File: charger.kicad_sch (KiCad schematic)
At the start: 0 parts

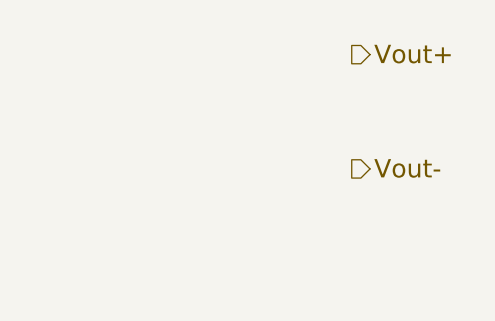
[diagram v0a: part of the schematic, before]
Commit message: Add analog schematic and refine wiring on top.
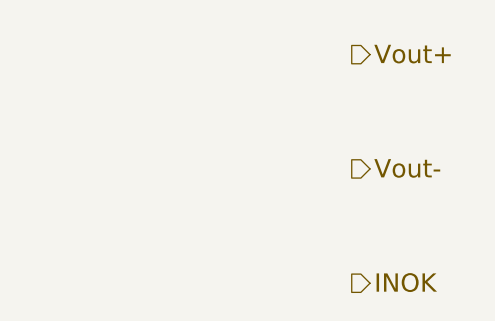
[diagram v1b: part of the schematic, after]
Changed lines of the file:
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@@
+		)
+	)
+	(hierarchical_label "INOK"
+		(shape output)
+		(at 254 63.5 0)
+		(effects
+			(font
+				(size 2.032 2.032)
+			)
+			(justify left)
 		)
 	)

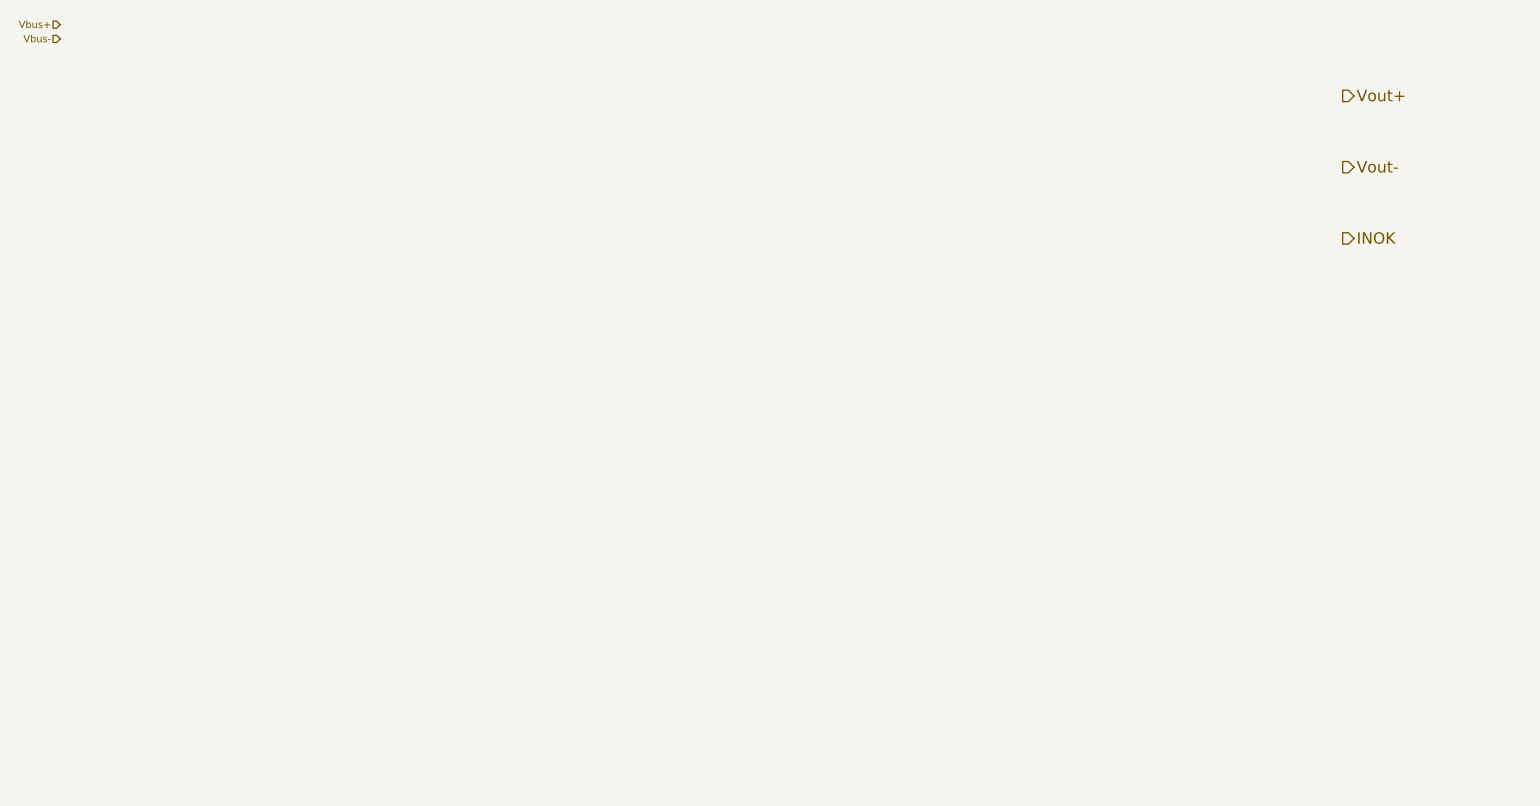
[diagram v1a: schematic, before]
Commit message: Add charger, battery cell.
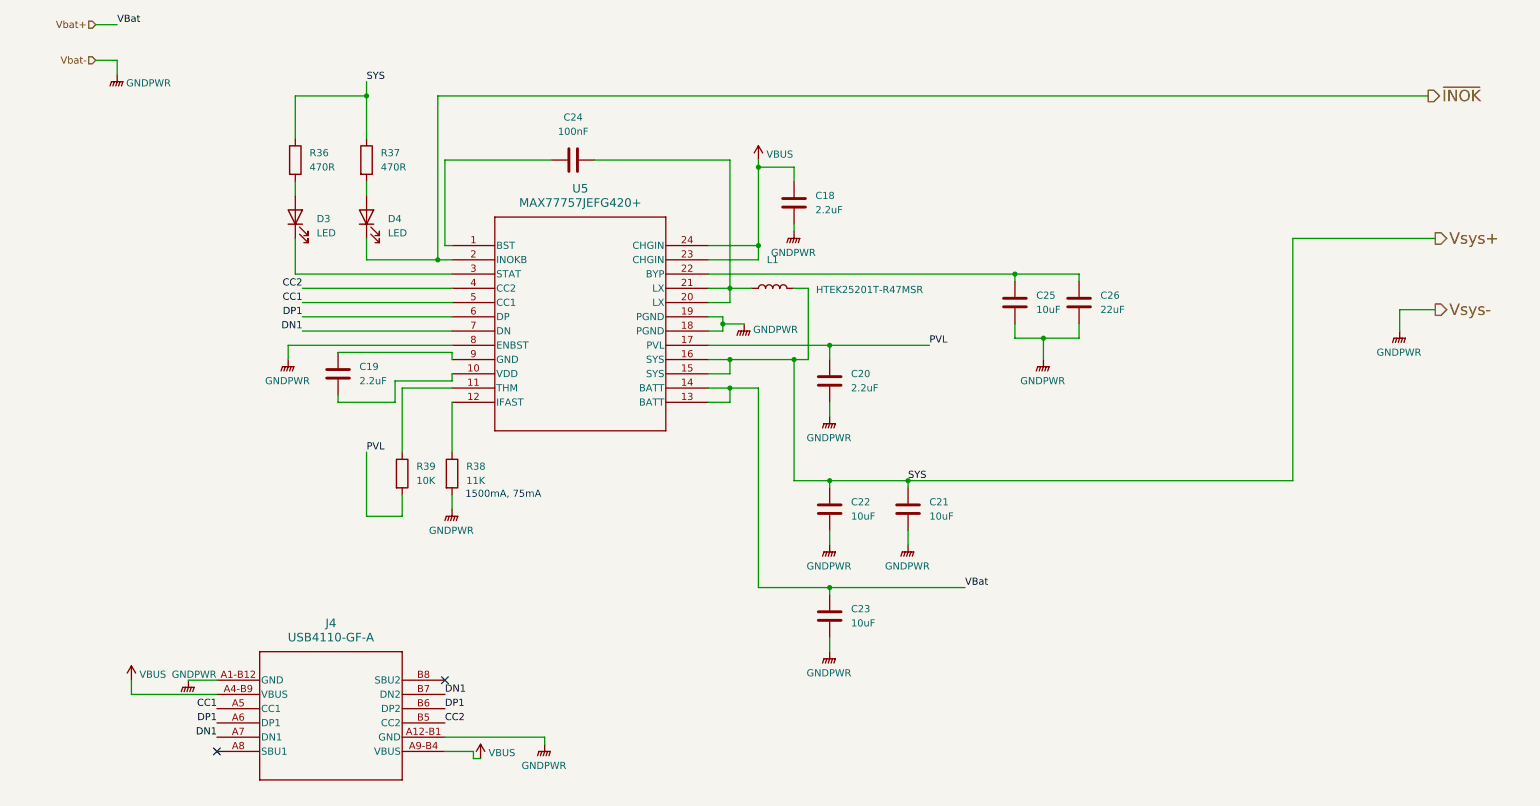
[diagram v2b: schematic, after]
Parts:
- added C18, C19, C20: 2.2uF, Capacitor_SMD:C_0603_1608Metric_Pad1.08x0.95mm_HandSolder, symbol Device:C
- added C21, C22, C23, C25: 10uF, Capacitor_SMD:C_0603_1608Metric_Pad1.08x0.95mm_HandSolder, symbol Device:C
- added C24: 100nF, Capacitor_SMD:C_0603_1608Metric_Pad1.08x0.95mm_HandSolder, symbol Device:C
- added C26: 22uF, Capacitor_SMD:C_0603_1608Metric_Pad1.08x0.95mm_HandSolder, symbol Device:C
- added D3, D4: LED, symbol Device:LED
- added J4: USB4110-GF-A, custom:USB4110-GF-A_GCT, symbol custom:USB4110-GF-A
- added L1: HTEK25201T-R47MSR, Inductor_SMD:L_1008_2520Metric_Pad1.43x2.20mm_HandSolder, symbol Device:L
- added R36, R37: 470R, Resistor_SMD:R_0603_1608Metric_Pad0.98x0.95mm_HandSolder, symbol Device:R
- added R38: 11K, Resistor_SMD:R_0603_1608Metric_Pad0.98x0.95mm_HandSolder, symbol Device:R
- added R39: 10K, Resistor_SMD:R_0603_1608Metric_Pad0.98x0.95mm_HandSolder, symbol Device:R
- added U5: MAX77757JEFG420+, 21-100385B_90-100128_MXM, symbol custom:MAX77757HEFG360+
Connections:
- new net: R38.1, U5.12 (IFAST)
- new net: C25.2, C26.2, U5.22 (BYP)
- new net: D3.2 (A), R36.2
- new net: R39.1, U5.11 (THM)
- new net: C19.1, U5.10 (VDD)
- new net: C19.2, U5.9 (GND)
- new net: D4.2 (A), R37.2
- new net: D3.1 (K), U5.3 (STAT)
- new net: C24.1, L1.1, U5.20 (LX), U5.21 (LX)
- new net: C24.2, U5.1 (BST)
- new net CC1: J4.A5 (CC1), U5.5 (CC1)
- new net CC2: J4.B5 (CC2), U5.4 (CC2)
- new net DN1: J4.A7 (DN1), J4.B7 (DN2), U5.7 (DN)
- new net DP1: J4.A6 (DP1), J4.B6 (DP2), U5.6 (DP)
- new net GNDPWR: C18.1, C20.1, C21.1, C22.1, C23.1, C25.1, C26.1, J4.A1-B12 (GND), J4.A12-B1 (GND), R38.2, U5.18 (PGND), U5.19 (PGND), U5.8 (ENBST)
- new net PVL: C20.2, R39.2, U5.17 (PVL)
- new net VBUS: C18.2, J4.A4-B9 (VBUS), J4.A9-B4 (VBUS), U5.23 (CHGIN), U5.24 (CHGIN)
- new net Vbat+: C23.2, U5.13 (BATT), U5.14 (BATT)
- new net Vsys+: C21.2, C22.2, L1.2, R36.1, R37.1, U5.15 (SYS), U5.16 (SYS)
- new net ~{INOK}: D4.1 (K), U5.2 (INOKB)
- no-connect marks 0 -> 2
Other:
- note added: "1500mA, 75mA"

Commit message: Add console port.
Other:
- note added: "This charger module circuit has not been tested yet."
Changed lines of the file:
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@@
+		)
+	)
+	(text "This charger module circuit has not been tested yet."
+		(exclude_from_sim no)
+		(at 203.708 161.544 0)
+		(effects
+			(font
+				(size 1.27 1.27)
+				(color 194 0 0 1)
+			)
 		)
 	)

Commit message: Fix issues
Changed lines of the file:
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@@
 		(dnp no)
 		(property "Reference" "L1"
-			(at 152.4 67.31 90)
+			(at 160.274 70.866 90)
 			(show_name no)
 			(do_not_autoplace no)

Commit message: Placement concept is finished.
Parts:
- D3, D4: footprint (none) -> LED_SMD:LED_0603_1608Metric
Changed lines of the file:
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@@
 			)
 		)
-		(property "Footprint" ""
+		(property "Footprint" "LED_SMD:LED_0603_1608Metric"
 			(at 80.01 59.69 0)
 			(hide yes)
@@
 			)
 		)
-		(property "Footprint" ""
+		(property "Footprint" "LED_SMD:LED_0603_1608Metric"
 			(at 67.31 59.69 0)
 			(hide yes)

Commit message: Add wiring, change footprint to avoid fatal errors at pads.
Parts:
- renumbered C19 to C18, C24 to C19, C18 to C20, C20 to C21, C21 to C24, D3 to D4, D4 to D5, J4 to J7, R36 to R32, R37 to R33, R39 to R34, R38 to R35
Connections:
- net GNDPWR: no longer U5.19 (PGND)
- net VBUS: no longer U5.24 (CHGIN)
- net Vbat+: no longer U5.14 (BATT)
- net Vsys+: no longer U5.16 (SYS)
- net at C19.1, L1.1, U5.20 (LX): no longer U5.21 (LX)

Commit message: Export BOM, change page headers.
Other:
- company: (none) -> B.Major
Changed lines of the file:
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@@
 	(generator_version "10.0")
 	(paper "A4")
+	(title_block
+		(date "2026-03-27")
+		(rev "1")
+		(company "B.Major")
+	)
 	(text "1500mA, 75mA"
 		(exclude_from_sim no)
